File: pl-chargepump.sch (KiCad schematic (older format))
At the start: 104 parts, among them J1 Prog, J2 Button, J4 Charger, J5 Seven-segment, J6 LOAD, Q1 MMBT2222A, Q2 MMBT2222A, Q3 MMBT2222A, Q4 MMBT2222A, Q5 MMBT2222A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

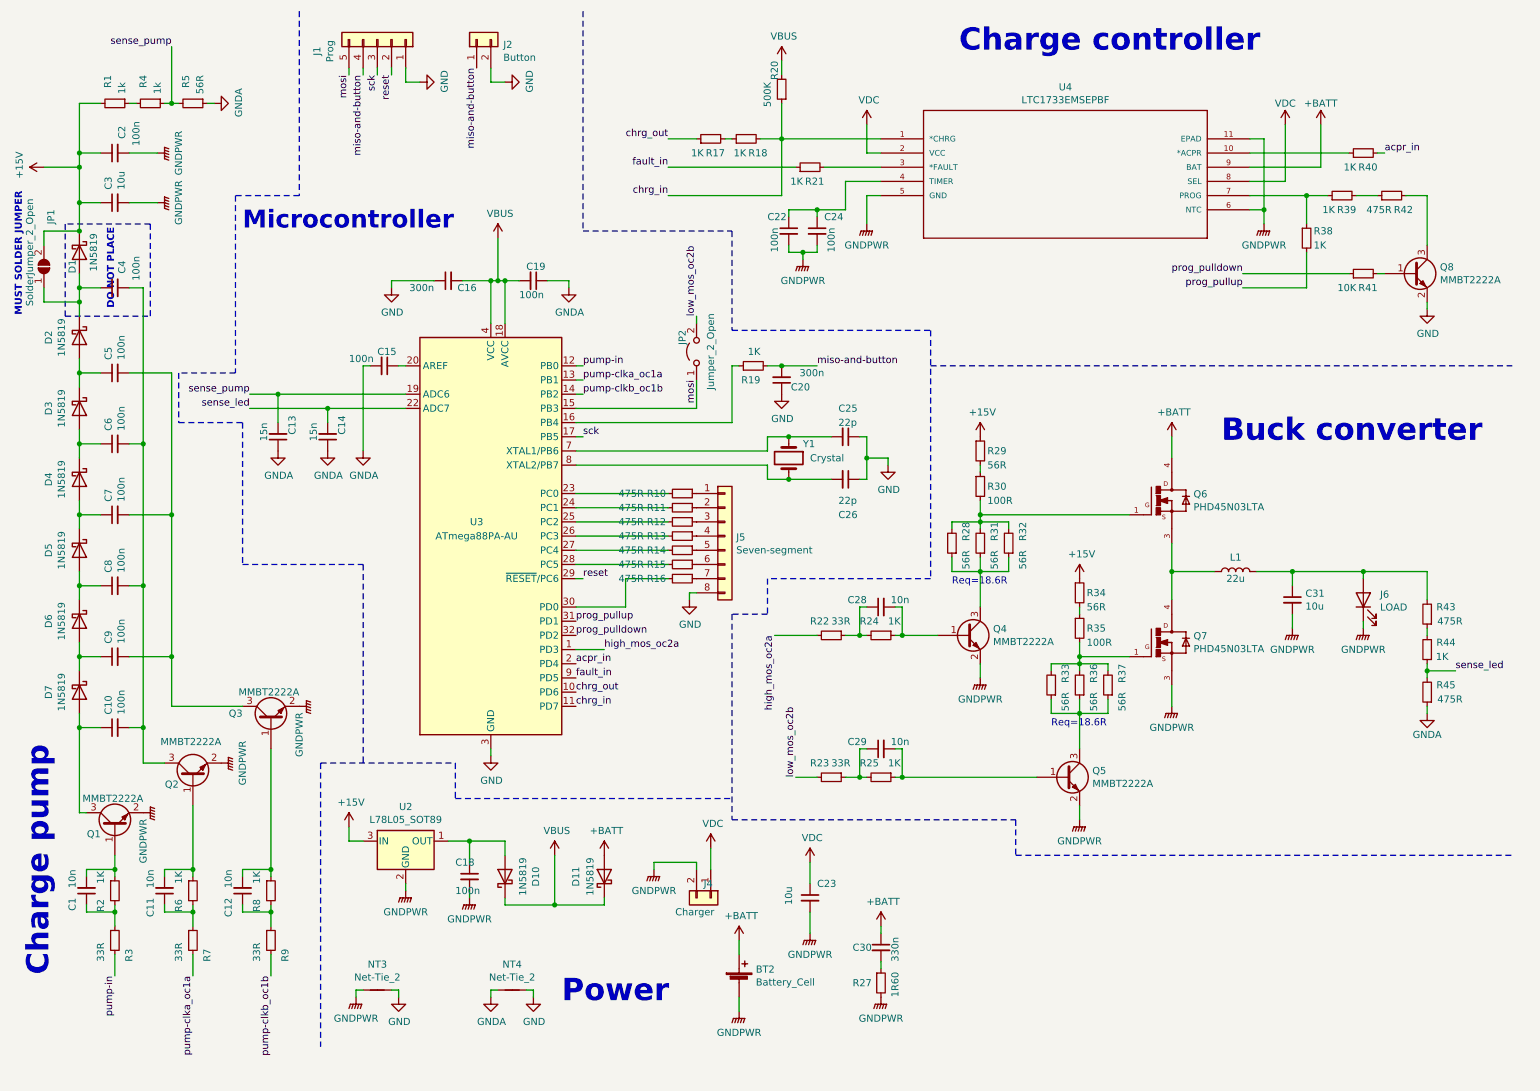
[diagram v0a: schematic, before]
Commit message: Fixed hierarchical sheet for microcontroller unit
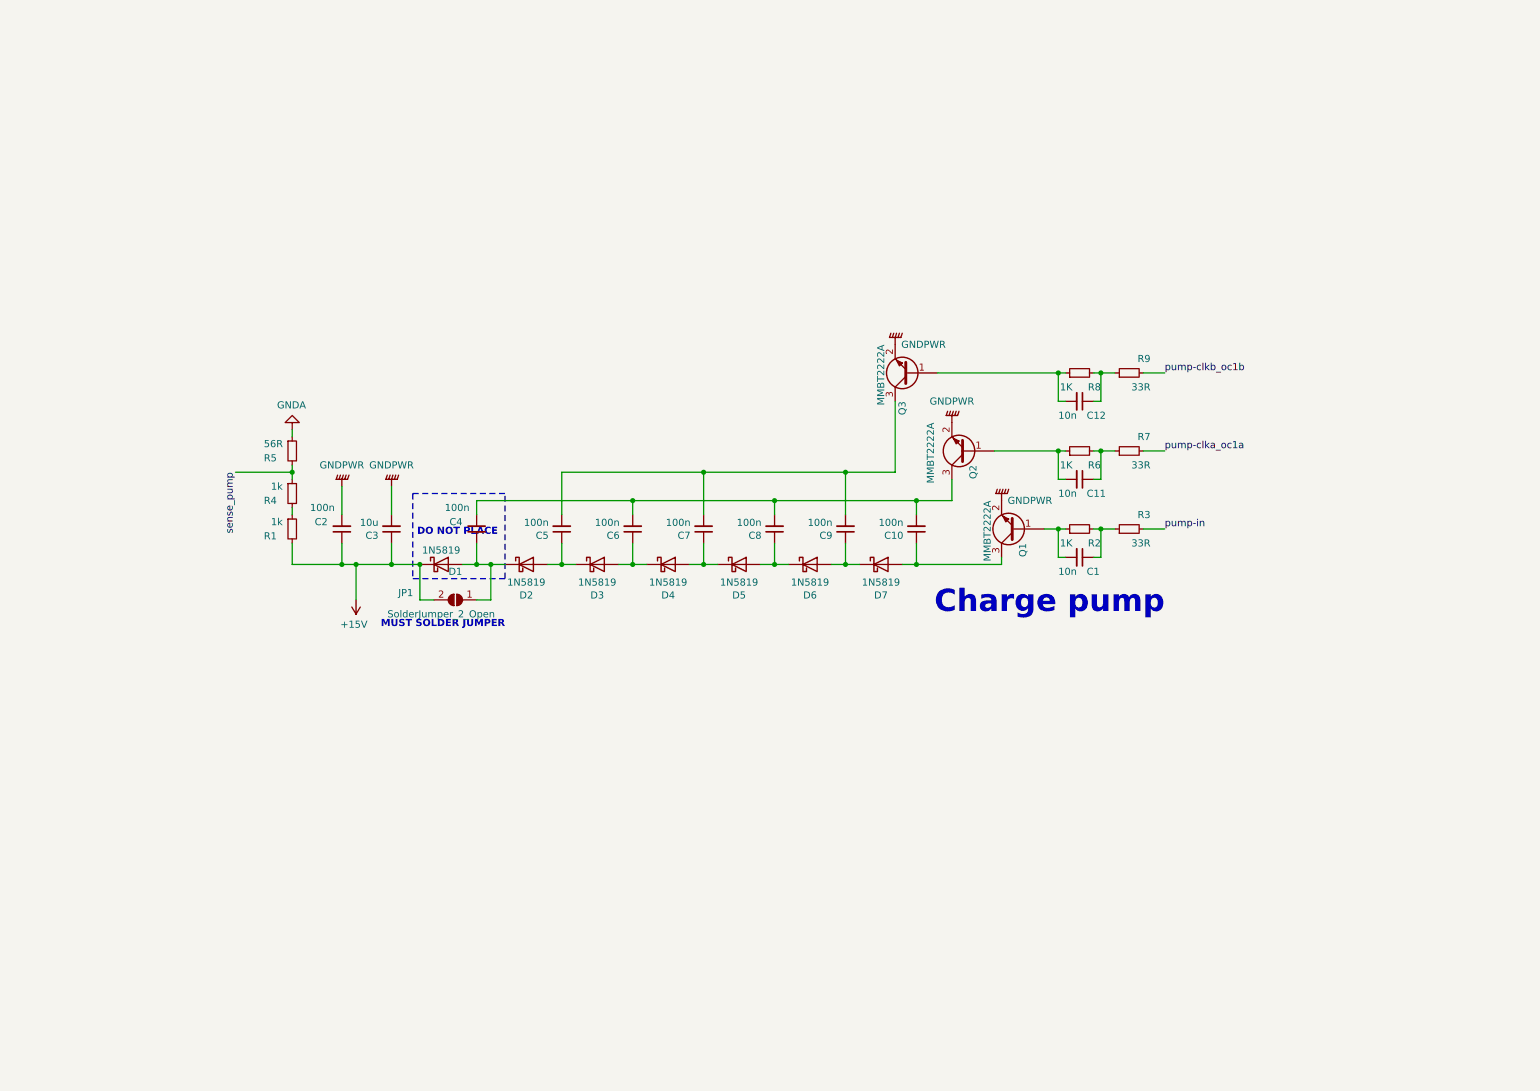
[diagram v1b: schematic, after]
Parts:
- removed BT2: Battery_Cell, Connector_PinHeader_2.54mm:PinHeader_1x02_P2.54mm_Vertical, symbol portable-light-rescue:Battery_Cell-Device
- removed C13, C14: 15n, Capacitor_SMD:C_1206_3216Metric_Pad1.42x1.75mm_HandSolder, symbol portable-light-rescue:C_Small-Device
- removed C15, C18, C19, C22, C24: 100n, Capacitor_SMD:C_1206_3216Metric_Pad1.42x1.75mm_HandSolder, symbol portable-light-rescue:C_Small-Device
- removed C16, C20: 300n, Capacitor_SMD:C_0805_2012Metric_Pad1.15x1.40mm_HandSolder, symbol portable-light-rescue:C_Small-Device
- removed C23, C31: 10u, Capacitor_THT:C_Radial_D5.0mm_H7.0mm_P2.00mm, symbol portable-light-rescue:C_Small-Device
- removed C25, C26: 22p, Capacitor_SMD:C_1206_3216Metric_Pad1.42x1.75mm_HandSolder, symbol portable-light-rescue:C_Small-Device
- removed C28, C29: 10n, Capacitor_SMD:C_1206_3216Metric_Pad1.42x1.75mm_HandSolder, symbol portable-light-rescue:C_Small-Device
- removed C30: 330n, Capacitor_SMD:C_1206_3216Metric_Pad1.42x1.75mm_HandSolder, symbol portable-light-rescue:C_Small-Device
- removed D10, D11: 1N5819, Diode_THT:D_DO-41_SOD81_P12.70mm_Horizontal, symbol portable-light-rescue:1N5819-Diode
- removed J1: Prog, Connector_PinHeader_2.54mm:PinHeader_1x05_P2.54mm_Vertical, symbol portable-light-rescue:Conn_01x05-Connector_Generic
- removed J2: Button, Ribbon_Cable:Ribbon_2, symbol portable-light-rescue:Conn_01x02-Connector_Generic
- removed J4: Charger, Connector_PinHeader_2.54mm:PinHeader_1x02_P2.54mm_Vertical, symbol portable-light-rescue:Conn_01x02-Connector_Generic
- removed J5: Seven-segment, Ribbon_Cable:Ribbon_8, symbol portable-light-rescue:Conn_01x08-Connector_Generic
- removed J6: LOAD, Connector_PinHeader_2.54mm:PinHeader_1x02_P2.54mm_Vertical, symbol portable-light-rescue:LED-Device
- removed JP2: Jumper_2_Open, Jumper:SolderJumper-2_P1.3mm_Open_RoundedPad1.0x1.5mm, symbol portable-light-rescue:Jumper_2_Open-Jumper
- removed L1: 22u, Capacitor_THT:CP_Radial_D8.0mm_P5.00mm, symbol portable-light-rescue:L-Device
- removed NT3, NT4: Net-Tie_2, NetTie:NetTie-2_SMD_Pad0.5mm, symbol portable-light-rescue:Net-Tie_2-Device
- removed Q4, Q5, Q8: MMBT2222A, Package_TO_SOT_SMD:SOT-23, symbol portable-light-rescue:MMBT3904-Transistor_BJT
- removed Q6, Q7: PHD45N03LTA, UniX_Generic:DPAK, symbol portable-light-rescue:PHD45N03LTA-PHD45N03LTA
- removed R10, R11, R12, R13, R14, R15, R16, R42, R43: 475R, Resistor_SMD:R_1206_3216Metric_Pad1.42x1.75mm_HandSolder, symbol portable-light-rescue:R_Small-Device
- removed R17, R18, R19, R21, R24, R25, R38, R39, R40, R44: 1K, Resistor_SMD:R_0603_1608Metric_Pad1.05x0.95mm_HandSolder, symbol portable-light-rescue:R_Small-Device
- removed R20: 500K, Resistor_THT:R_Axial_DIN0309_L9.0mm_D3.2mm_P12.70mm_Horizontal, symbol portable-light-rescue:R_Small-Device
- removed R22, R23: 33R, Resistor_SMD:R_0805_2012Metric_Pad1.15x1.40mm_HandSolder, symbol portable-light-rescue:R_Small-Device
- removed R27: 1R60, Resistor_SMD:R_0805_2012Metric_Pad1.15x1.40mm_HandSolder, symbol portable-light-rescue:R_Small-Device
- removed R28, R29, R31, R32, R33, R34, R36, R37: 56R, Resistor_SMD:R_0805_2012Metric_Pad1.15x1.40mm_HandSolder, symbol portable-light-rescue:R_Small-Device
- removed R30, R35: 100R, Resistor_SMD:R_1206_3216Metric_Pad1.42x1.75mm_HandSolder, symbol portable-light-rescue:R_Small-Device
- removed R41: 10K, Resistor_SMD:R_1206_3216Metric_Pad1.42x1.75mm_HandSolder, symbol portable-light-rescue:R_Small-Device
- removed R45: 475R, Resistor_SMD:R_0805_2012Metric_Pad1.15x1.40mm_HandSolder, symbol portable-light-rescue:R_Small-Device
- removed U2: L78L05_SOT89, Package_TO_SOT_SMD:SOT-89-3, symbol portable-light-rescue:L78L05_SOT89-Regulator_Linear
- removed U3: ATmega88PA-AU, Package_QFP:TQFP-32_7x7mm_P0.8mm, symbol portable-light-rescue:ATmega88PA-AU-MCU_Microchip_ATmega
- removed U4: LTC1733EMSEPBF, UniX_Generic:MSOP-10_MSE, symbol portable-light-rescue:LTC1733EMSEPBF-LTC1733
- removed Y1: Crystal, Crystal:Crystal_SMD_HC49-SD, symbol portable-light-rescue:Crystal-Device
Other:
- note removed: "Buck converter"
- note removed: "Charge controller"
- note removed: "Microcontroller"
- note removed: "Power"
- note removed: "Req=18.6R"
- moved on the sheet: C1, C10, C11, C12, C2, C3, C4, C5, C6, C7, C8, C9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

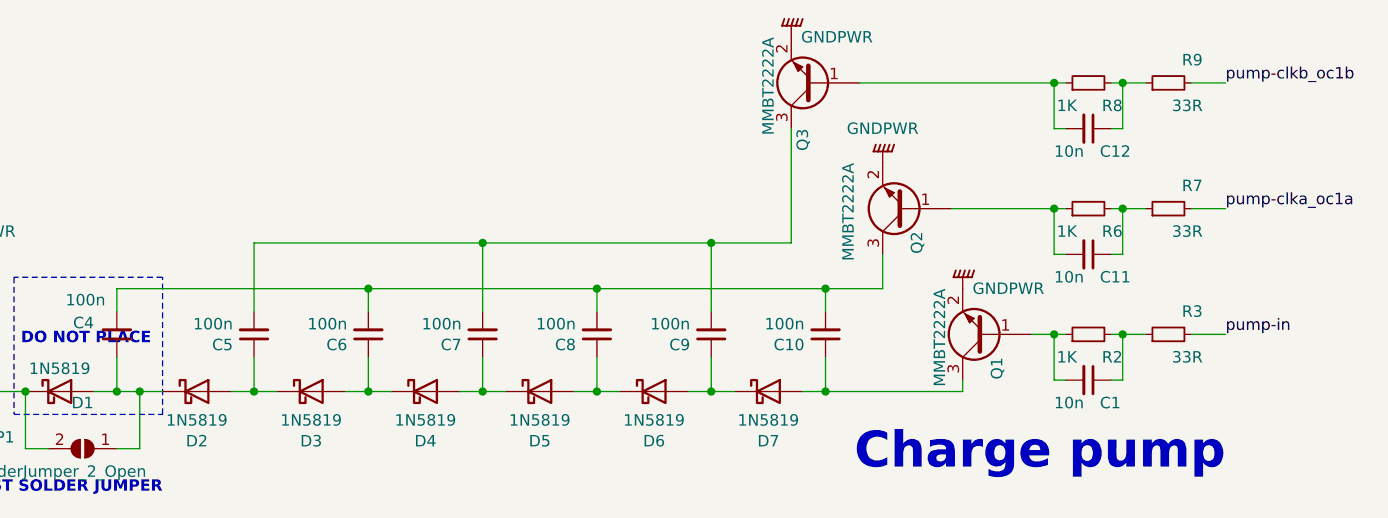
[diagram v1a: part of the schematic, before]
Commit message: Charger hierarchical sheet fixed
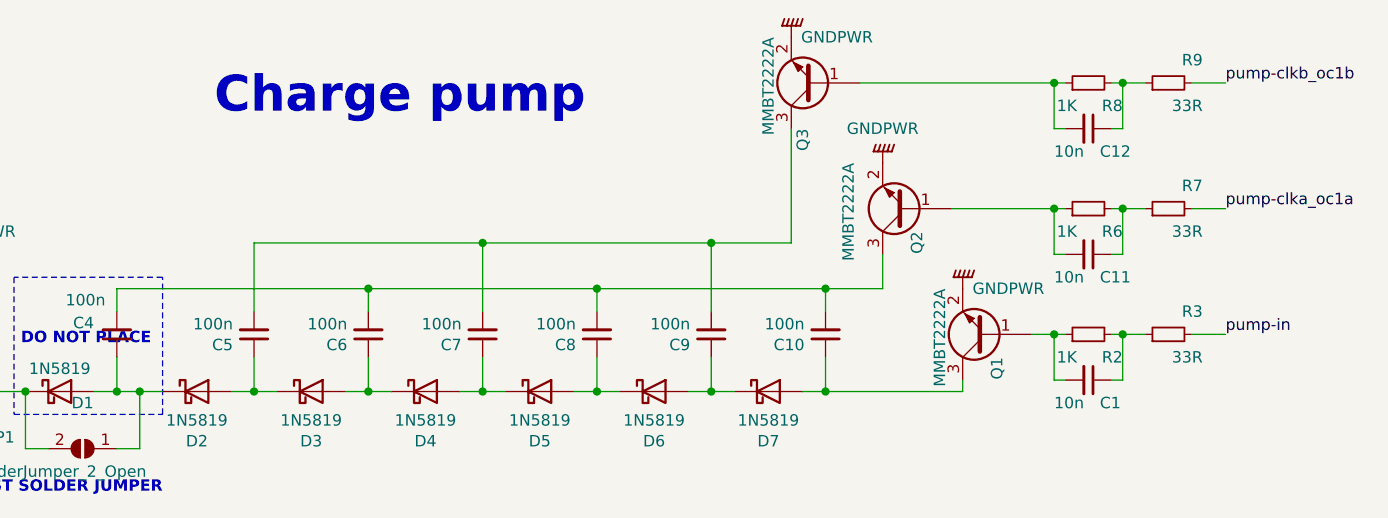
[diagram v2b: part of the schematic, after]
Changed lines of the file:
@@
 Wire Wire Line
 	7950 4350 7950 4150
-Text Notes 8700 4757 2    157  ~ 31
+Text Notes 5900 3200 2    157  ~ 31
 Charge pump
 Wire Wire Line
